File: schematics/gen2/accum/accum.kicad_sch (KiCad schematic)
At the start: 15 parts, among them U1 74LS574, U2 74LS138, U3 74LS02, U4 74LS245, U5 74LS245, U6 74LS245

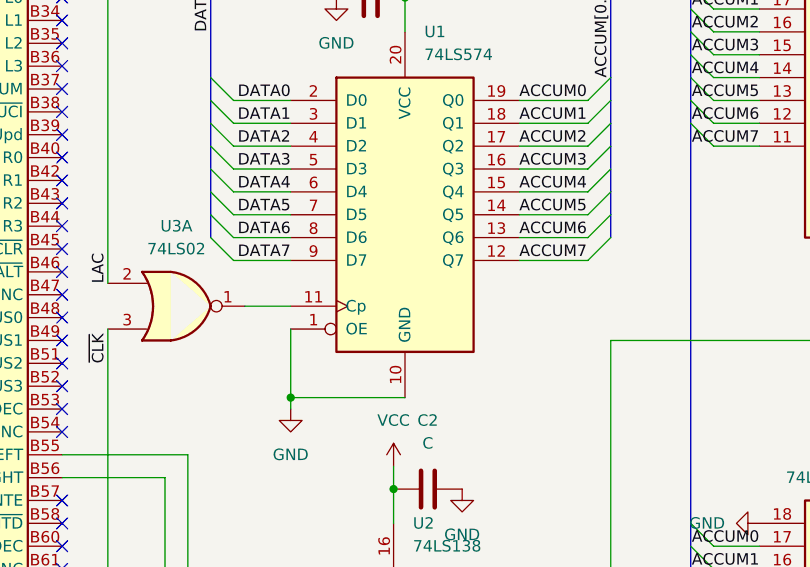
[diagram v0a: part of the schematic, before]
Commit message: fix: update accumulator schematic and routing rules
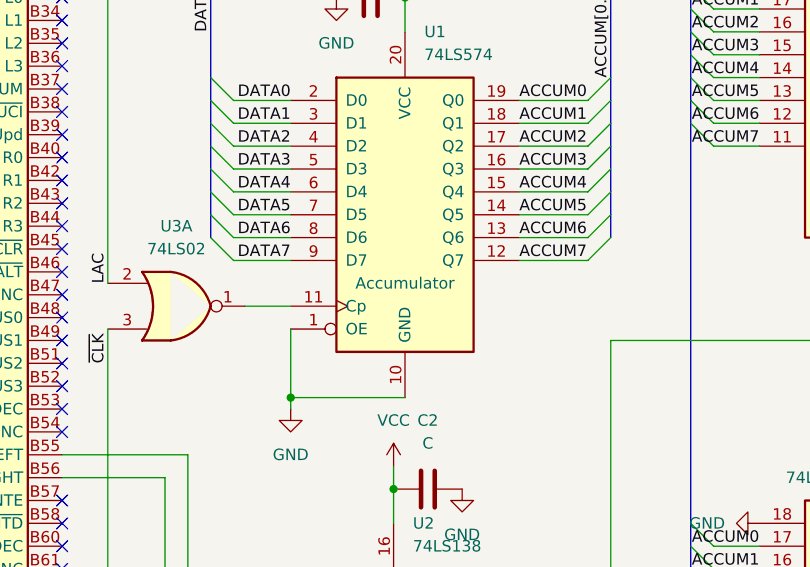
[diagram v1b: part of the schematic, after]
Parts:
- U1: Type (none) -> Accumulator
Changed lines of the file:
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@@
 		(on_board yes)
 		(dnp no)
-		(fields_autoplaced yes)
 		(property "Reference" "U1"
 			(at 101.2033 38.1 0)
@@
 			)
 		)
+		(property "Type" "Accumulator"
+			(at 99.06 66.04 0)
+			(effects
+				(font
+					(size 1.27 1.27)
+				)
+			)
+		)

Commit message: fix: changed footprints in accum, added resistor and capacitor footrpint
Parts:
- C1, C2, C3, C4, C5, C6: footprint Capacitor_SMD:C_0805_2012Metric_Pad1.18x1.45mm_HandSolder -> Capacitor_THT:C_Disc_D3.0mm_W1.6mm_P2.50mm
- C7: footprint Capacitor_SMD:C_0805_2012Metric_Pad1.18x1.45mm_HandSolder -> Capacitor_THT:C_Radial_D6.3mm_H5.0mm_P2.50mm
- R1: footprint (none) -> Resistor_THT:R_Axial_DIN0207_L6.3mm_D2.5mm_P7.62mm_Horizontal
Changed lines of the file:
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@@
 			)
 		)
-		(property "Footprint" ""
+		(property "Footprint" "Resistor_THT:R_Axial_DIN0207_L6.3mm_D2.5mm_P7.62mm_Horizontal"
 			(at 81.28 114.808 90)
 			(effects
@@
 			)
 		)
-		(property "Footprint" "Capacitor_SMD:C_0805_2012Metric_Pad1.18x1.45mm_HandSolder"
+		(property "Footprint" "Capacitor_THT:C_Disc_D3.0mm_W1.6mm_P2.50mm"
 			(at 158.75 81.5848 0)
 			(effects
@@
 			)
 		)
-		(property "Footprint" "Capacitor_SMD:C_0805_2012Metric_Pad1.18x1.45mm_HandSolder"
+		(property "Footprint" "Capacitor_THT:C_Disc_D3.0mm_W1.6mm_P2.50mm"
 			(at 91.44 33.3248 0)
 			(effects
@@
 		(at 49.53 22.86 90)
 		(unit 1)
-		(exclude_from_sim no)
+		(exclude_from_sim yes)
 		(in_bom yes)
 		(on_board yes)
@@
 			)
 		)
-		(property "Footprint" "Capacitor_SMD:C_0805_2012Metric_Pad1.18x1.45mm_HandSolder"
+		(property "Footprint" "Capacitor_THT:C_Radial_D6.3mm_H5.0mm_P2.50mm"
 			(at 53.34 21.8948 0)
 			(effects
@@
 			)
 		)
-		(property "Footprint" "Capacitor_SMD:C_0805_2012Metric_Pad1.18x1.45mm_HandSolder"
+		(property "Footprint" "Capacitor_THT:C_Disc_D3.0mm_W1.6mm_P2.50mm"
 			(at 105.41 87.9348 0)
 			(effects
@@
 			)
 		)
-		(property "Footprint" "Capacitor_SMD:C_0805_2012Metric_Pad1.18x1.45mm_HandSolder"
+		(property "Footprint" "Capacitor_THT:C_Disc_D3.0mm_W1.6mm_P2.50mm"
 			(at 158.75 145.0848 0)
 			(effects
@@
 			)
 		)
-		(property "Footprint" "Capacitor_SMD:C_0805_2012Metric_Pad1.18x1.45mm_HandSolder"
+		(property "Footprint" "Capacitor_THT:C_Disc_D3.0mm_W1.6mm_P2.50mm"
 			(at 99.06 155.2448 0)
 			(effects
@@
 			)
 		)
-		(property "Footprint" "Capacitor_SMD:C_0805_2012Metric_Pad1.18x1.45mm_HandSolder"
+		(property "Footprint" "Capacitor_THT:C_Disc_D3.0mm_W1.6mm_P2.50mm"
 			(at 158.75 21.8948 0)
 			(effects

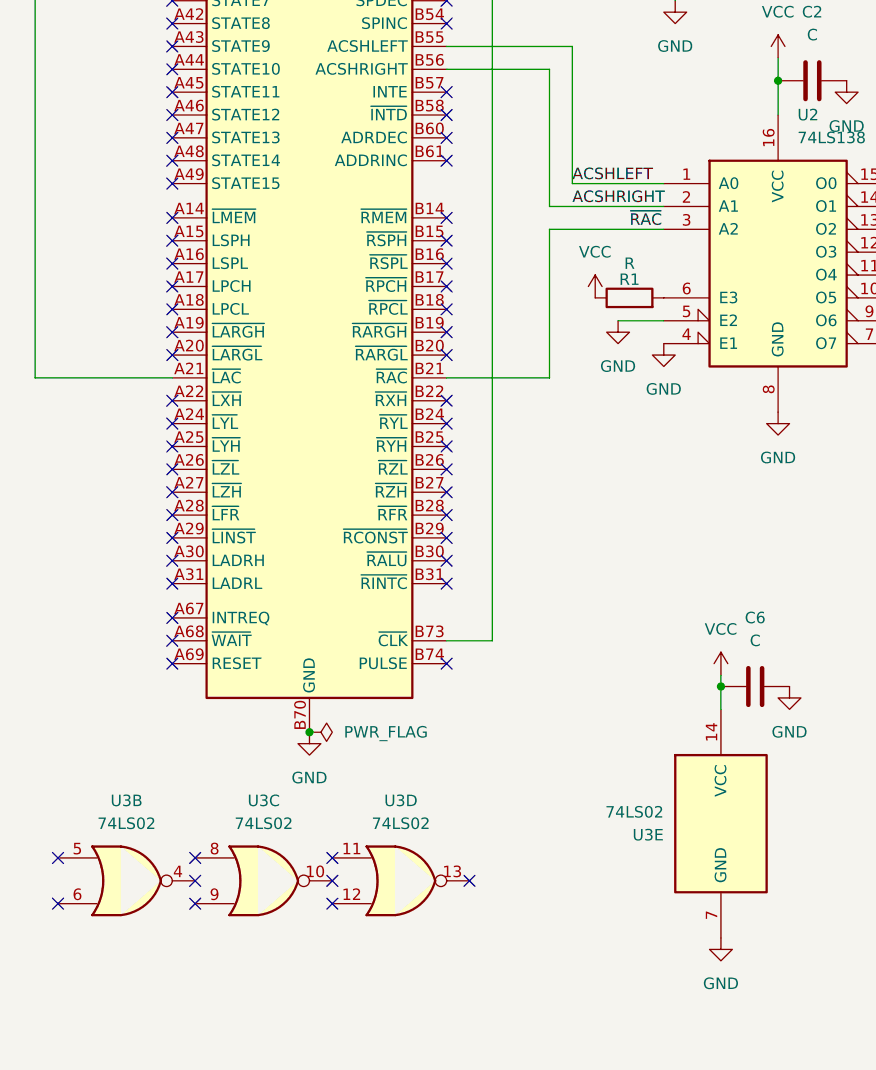
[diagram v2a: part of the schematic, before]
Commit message: refactor(accum): reimplemented accumalot module
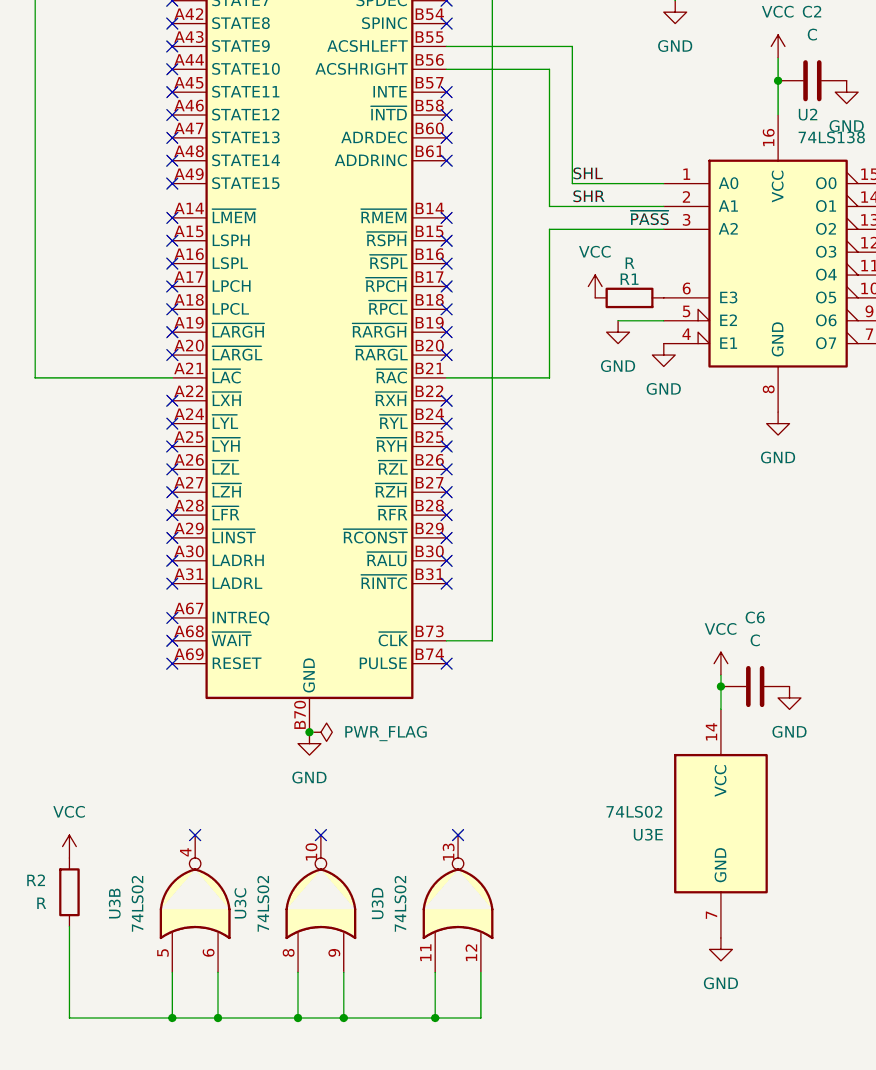
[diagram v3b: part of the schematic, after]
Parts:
- added R2: R, Resistor_THT:R_Axial_DIN0207_L6.3mm_D2.5mm_P7.62mm_Horizontal, symbol Device:R
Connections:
- net ACSHLEFT: no longer BC1.B55 (ACSHLEFT), U2.1 (A0)
- net ACSHRIGHT: no longer BC1.B56 (ACSHRIGHT), U2.2 (A1)
- net VCC: now also R2.2
- net ~{RAC}: no longer BC1.B21 (~{RAC}), U2.3 (A2)
- net at U3.5: now also U3.11, U3.12, U3.6, U3.8, U3.9, R2.1
- new net SHL: BC1.B55 (ACSHLEFT), U2.1 (A0)
- new net SHR: BC1.B56 (ACSHRIGHT), U2.2 (A1)
- new net ~{PASS}: BC1.B21 (~{RAC}), U2.3 (A2)
- no-connect marks 95 -> 89
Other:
- moved on the sheet: U3B, U3C, U3D

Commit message: accum review complete
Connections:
- no-connect marks 89 -> 87
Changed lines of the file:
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@@
 	)
 	(no_connect
-		(at 138.43 153.67)
-	)
-	(no_connect
 		(at 60.96 59.69)
 	)
@@
 	)
 	(no_connect
-		(at 138.43 113.03)
-	)
-	(no_connect
 		(at 60.96 34.29)
 	)
@@
 	)
 	(bus_entry
-		(at 130.81 110.49)
-		(size 2.54 2.54)
-		(stroke
-			(width 0)
-			(type default)
-		)
-	)
-	(bus_entry
 		(at 77.47 60.96)
 		(size 2.54 2.54)
@@
 	)
 	(bus_entry
-		(at 130.81 151.13)
-		(size 2.54 2.54)
-		(stroke
-			(width 0)
-			(type default)
-		)
-	)
-	(bus_entry
 		(at 172.72 100.33)
 		(size -2.54 2.54)
@@
 	(bus
 		(pts
-			(xy 130.81 107.95) (xy 130.81 110.49)
-		)
-		(stroke
-			(width 0)
-			(type default)
-		)
-	)
-	(bus
-		(pts
 			(xy 172.72 156.21) (xy 172.72 158.75)
 		)
@@
 	(wire
 		(pts
-			(xy 133.35 153.67) (xy 138.43 153.67)
-		)
-		(stroke
-			(width 0)
-			(type default)
-		)
-	)
-	(wire
-		(pts
 			(xy 133.35 40.64) (xy 138.43 40.64)
 		)
@@
 		)
 	)
-	(wire
-		(pts
-			(xy 133.35 113.03) (xy 138.43 113.03)
-		)
-		(stroke
-			(width 0)
-			(type default)
-		)
-	)
 	(bus
 		(pts
@@
 	(bus
 		(pts
-			(xy 130.81 151.13) (xy 130.81 153.67)
+			(xy 130.81 107.95) (xy 130.81 153.67)
 		)
 		(stroke
@@
 		)
 	)
-	(bus
-		(pts
-			(xy 130.81 110.49) (xy 130.81 151.13)
-		)
-		(stroke
-			(width 0)
-			(type default)
-		)
-	)
 	(wire
 		(pts
@@
 		)
 	)
-	(label "ACCUM7"
-		(at 138.43 113.03 180)
-		(effects
-			(font
-				(size 1.27 1.27)
-			)
-			(justify right bottom)
-		)
-	)
 	(label "ACCUM2"
 		(at 138.43 158.75 180)
@@
 		(effects
 			(font
-				(size 1.27 1.27)
-			)
-			(justify right bottom)
-		)
-	)
-	(label "ACCUM0"
-		(at 138.43 153.67 180)
-		(effects
-			(font

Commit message: accum schematic
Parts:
- C1, C2, C3, C4, C5, C6: footprint Capacitor_THT:C_Disc_D3.0mm_W1.6mm_P2.50mm -> Capacitor_THT:C_Disc_D5.0mm_W2.5mm_P5.00mm
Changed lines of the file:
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@@
 			)
 		)
-		(property "Footprint" "Capacitor_THT:C_Disc_D3.0mm_W1.6mm_P2.50mm"
+		(property "Footprint" "Capacitor_THT:C_Disc_D5.0mm_W2.5mm_P5.00mm"
 			(at 158.75 81.5848 0)
 			(effects
@@
 			)
 		)
-		(property "Footprint" "Capacitor_THT:C_Disc_D3.0mm_W1.6mm_P2.50mm"
+		(property "Footprint" "Capacitor_THT:C_Disc_D5.0mm_W2.5mm_P5.00mm"
 			(at 91.44 33.3248 0)
 			(effects
@@
 			)
 		)
-		(property "Footprint" "Capacitor_THT:C_Disc_D3.0mm_W1.6mm_P2.50mm"
+		(property "Footprint" "Capacitor_THT:C_Disc_D5.0mm_W2.5mm_P5.00mm"
 			(at 105.41 87.9348 0)
 			(effects
@@
 			)
 		)
-		(property "Footprint" "Capacitor_THT:C_Disc_D3.0mm_W1.6mm_P2.50mm"
+		(property "Footprint" "Capacitor_THT:C_Disc_D5.0mm_W2.5mm_P5.00mm"
 			(at 158.75 145.0848 0)
 			(effects
@@
 			)
 		)
-		(property "Footprint" "Capacitor_THT:C_Disc_D3.0mm_W1.6mm_P2.50mm"
+		(property "Footprint" "Capacitor_THT:C_Disc_D5.0mm_W2.5mm_P5.00mm"
 			(at 99.06 155.2448 0)
 			(effects
@@
 			)
 		)
-		(property "Footprint" "Capacitor_THT:C_Disc_D3.0mm_W1.6mm_P2.50mm"
+		(property "Footprint" "Capacitor_THT:C_Disc_D5.0mm_W2.5mm_P5.00mm"
 			(at 158.75 21.8948 0)
 			(effects
